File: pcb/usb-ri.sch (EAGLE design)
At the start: 43 parts, among them IC1 STM32F303, IC2 REG1117, IC3 STF203-22, IC4 FT231XS-R, J1 JTAG, J2 MJ-3536, J3 RESET, J4 10118193-0001LF, Q1 IRLML9303, Q2 IRLML2030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

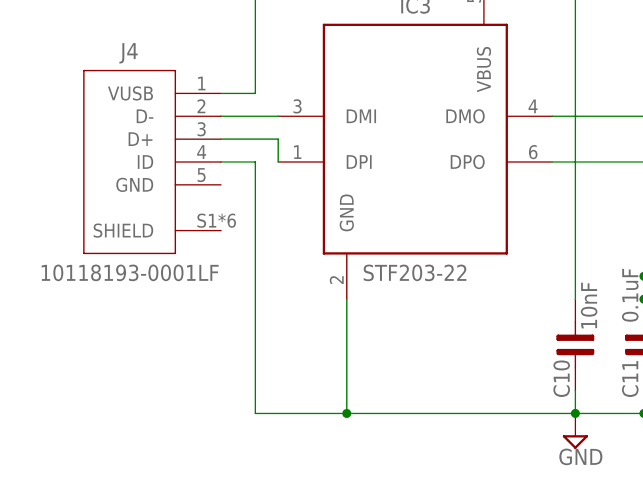
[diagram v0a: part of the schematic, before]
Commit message: Fixed PCB bug: connection of USB port
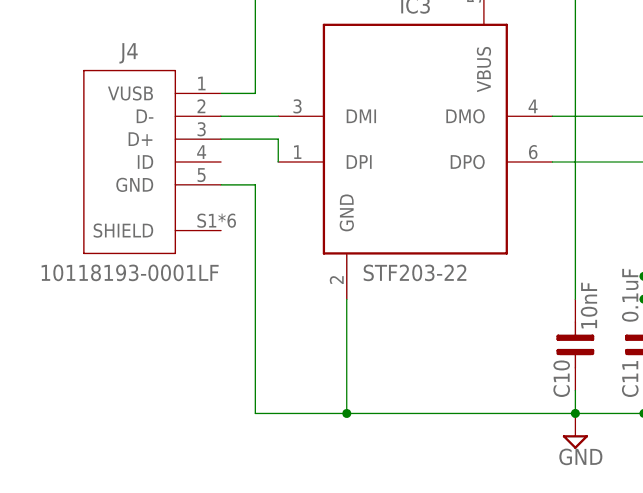
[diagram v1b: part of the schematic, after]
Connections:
- net GND: now also J4.GND; no longer J4.ID
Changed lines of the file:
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@@
 <setting verticaltext="up"/>
 </settings>
-<grid distance="0.1" unitdist="inch" unit="inch" style="lines" multiple="1" display="no" altdistance="0.01" altunitdist="inch" altunit="inch"/>
+<grid distance="0.05" unitdist="inch" unit="inch" style="lines" multiple="1" display="yes" altdistance="0.01" altunitdist="inch" altunit="inch"/>
 <layers>
 <layer number="1" name="Top" color="4" fill="1" visible="no" active="no"/>
@@
 <junction x="30.48" y="15.24"/>
 <pinref part="SUPPLY9" gate="GND" pin="GND"/>
-<pinref part="J4" gate="G$1" pin="ID"/>
-<wire x1="16.51" y1="43.18" x2="20.32" y2="43.18" width="0.1524" layer="91"/>
-<wire x1="20.32" y1="43.18" x2="20.32" y2="15.24" width="0.1524" layer="91"/>
 <pinref part="IC4" gate="G$1" pin="GND"/>
 <wire x1="55.88" y1="15.24" x2="63.5" y2="15.24" width="0.1524" layer="91"/>
@@
 <wire x1="63.5" y1="17.78" x2="63.5" y2="15.24" width="0.1524" layer="91"/>
 <junction x="63.5" y="15.24"/>
+<wire x1="20.32" y1="15.24" x2="20.32" y2="40.64" width="0.1524" layer="91"/>
+<pinref part="J4" gate="G$1" pin="GND"/>
+<wire x1="16.51" y1="40.64" x2="20.32" y2="40.64" width="0.1524" layer="91"/>
 </segment>
 <segment>
